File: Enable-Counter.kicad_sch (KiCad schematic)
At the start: 4 parts, among them SW1 SW_Push, U3 SN74LVC112AD, U4 74LVC1G04, U5 74LVC1G04

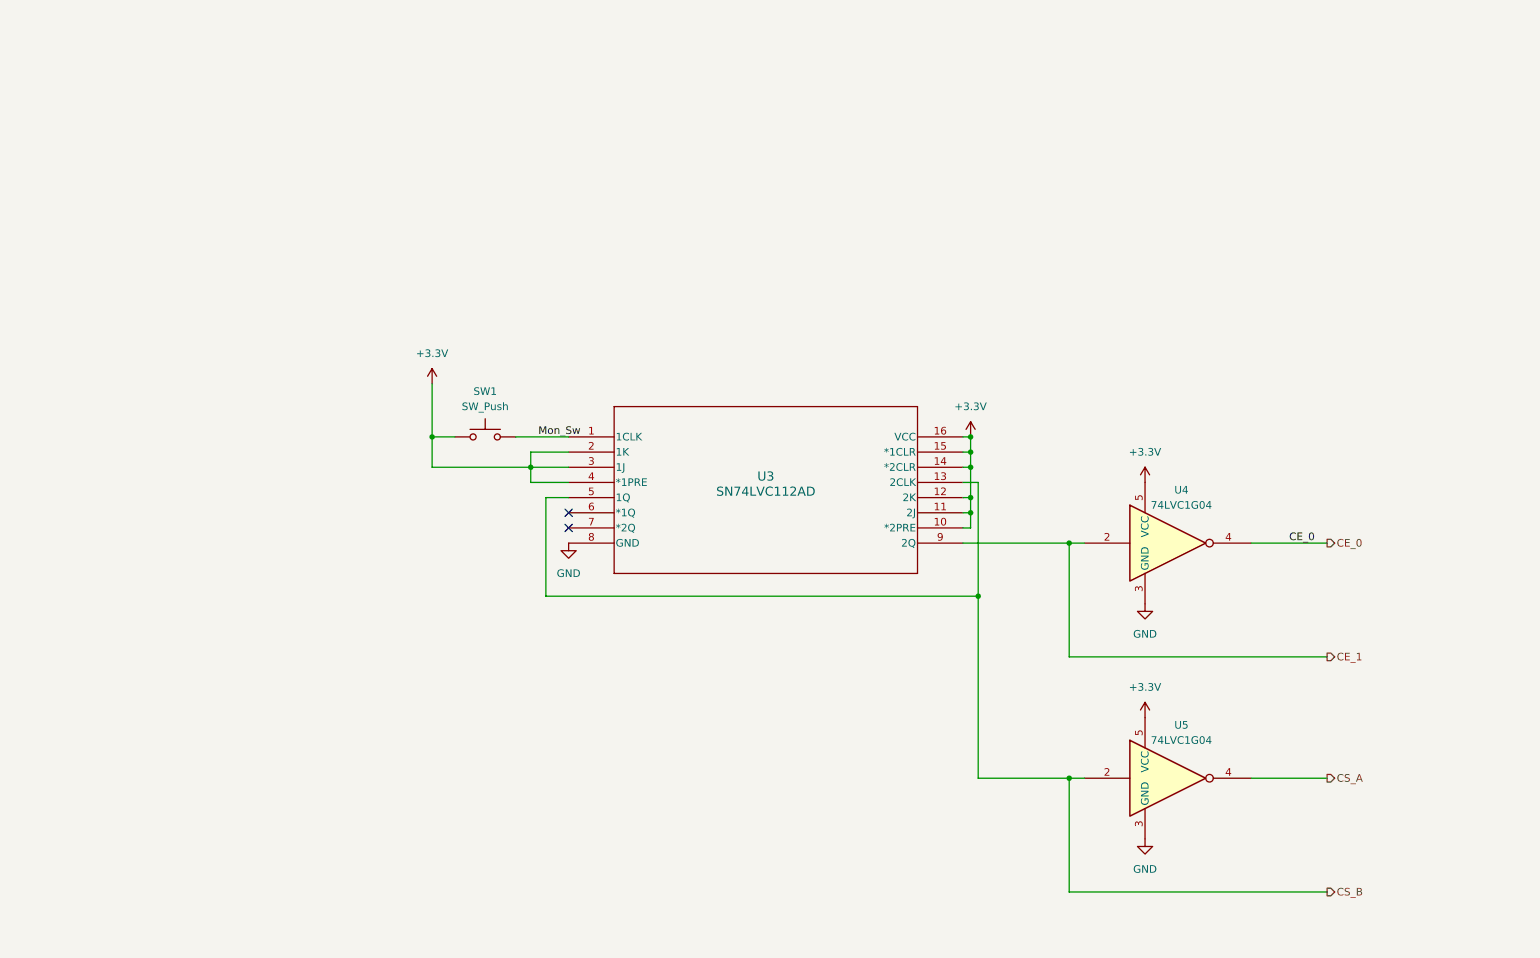
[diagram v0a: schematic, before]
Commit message: Switch debounce, input mDP to switch ICs
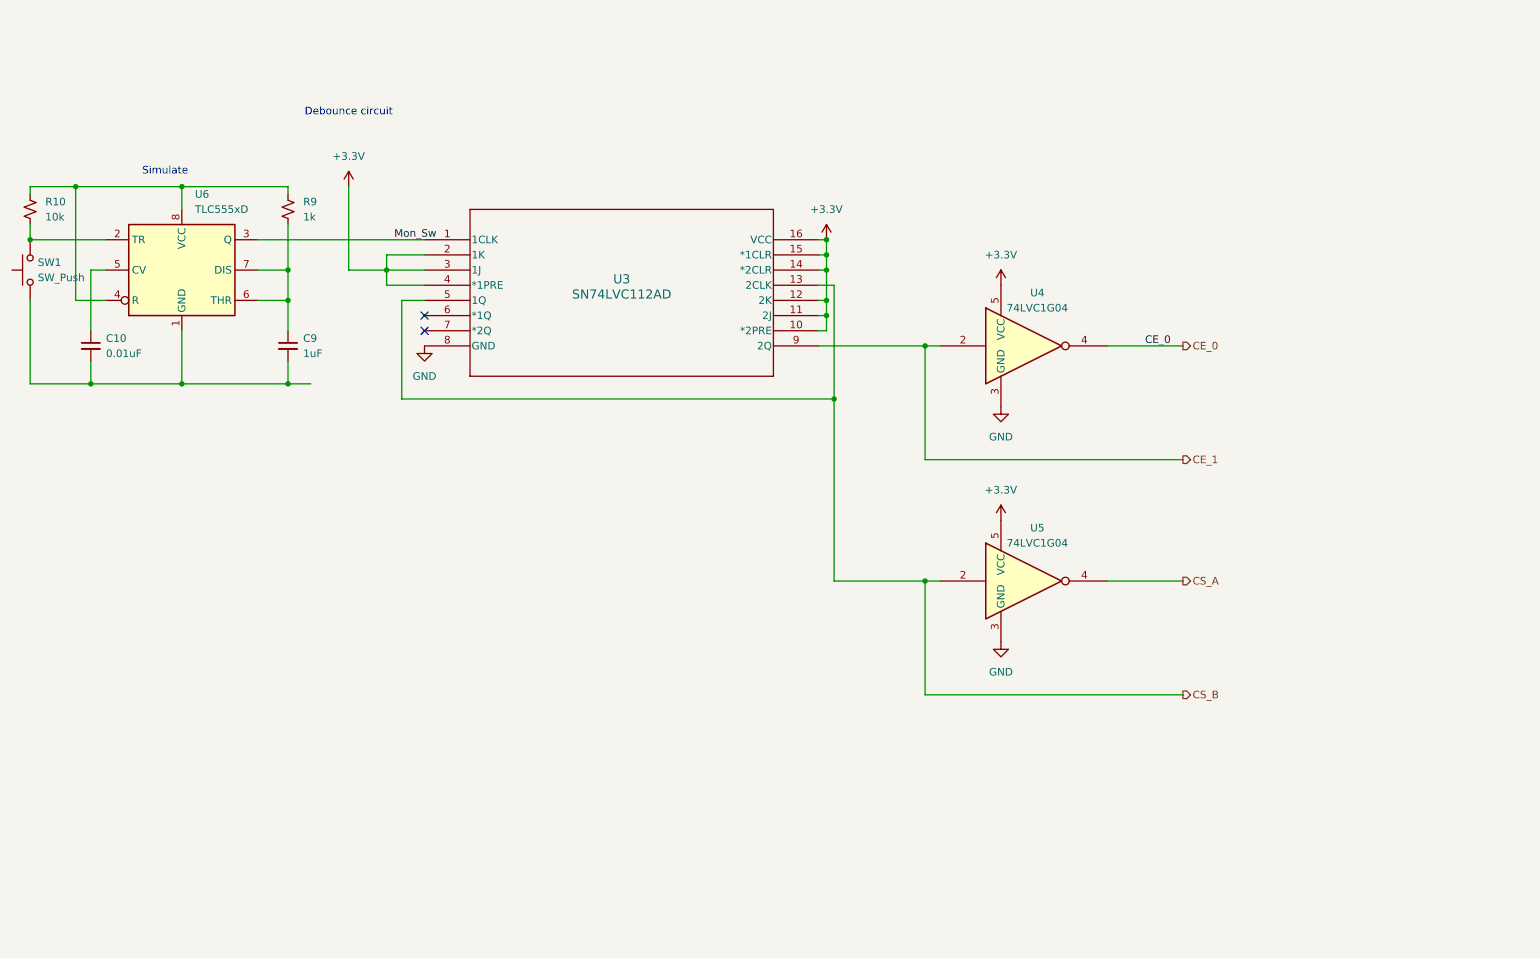
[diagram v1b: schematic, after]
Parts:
- added C10: 0.01uF, symbol Device:C_Small
- added C9: 1uF, symbol Device:C_Small
- added R10: 10k, symbol Device:R_Small_US
- added R9: 1k, symbol Device:R_Small_US
- added U6: TLC555xD, Package_SO:SOIC-8_3.9x4.9mm_P1.27mm, symbol Timer:TLC555xD
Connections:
- net +3.3V: no longer SW1.1
- net Mon_Sw: now also U6.3 (Q); no longer SW1.2
- new net: C10.2, C9.2, SW1.1, U6.1 (GND)
- new net: R10.2, SW1.2, U6.2 (TR)
- new net: C9.1, R9.2, U6.6 (THR), U6.7 (DIS)
- new net: R10.1, R9.1, U6.4 (R), U6.8 (VCC)
- new net: C10.1, U6.5 (CV)
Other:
- note added: "Debounce circuit"
- note added: "Simulate"
- moved on the sheet: U3, U4, U5

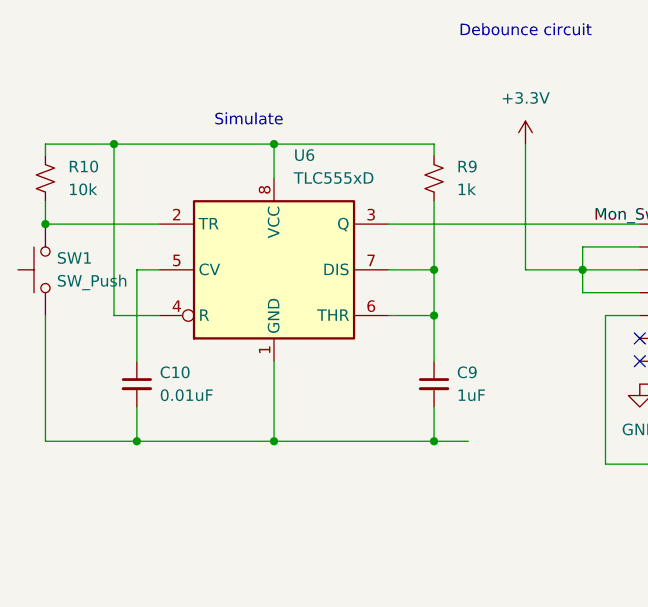
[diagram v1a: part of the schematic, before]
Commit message: Fix debounce circuit
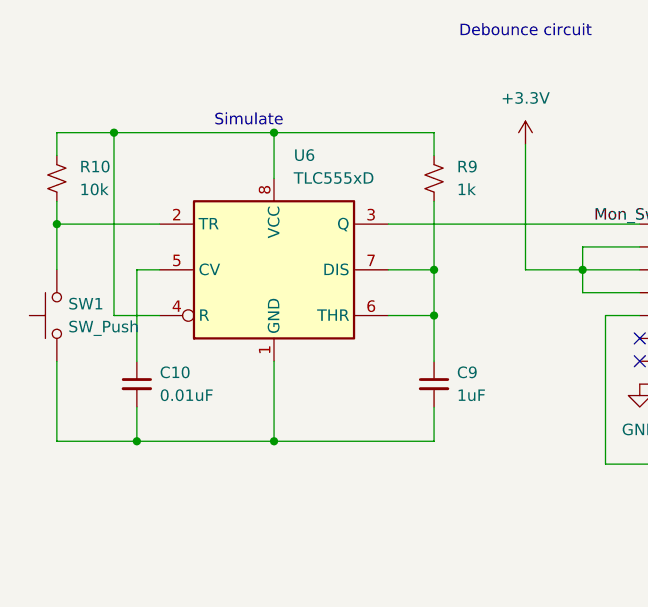
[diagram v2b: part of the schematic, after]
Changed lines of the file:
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@@
 	(paper "USLetter")
+	(junction
+		(at 41.91 41.91)
+		(diameter 0)
+		(color 0 0 0 0)
+	)
 	(junction
 		(at 149.86 57.15)
@@
 	)
 	(junction
+		(at 24.13 41.91)
+		(diameter 0)
+		(color 0 0 0 0)
+	)
+	(junction
 		(at 59.69 57.15)
 		(diameter 0)
@@
 	)
 	(junction
+		(at 17.78 52.07)
+		(diameter 0)
+		(color 0 0 0 0)
+	)
+	(junction
 		(at 151.13 78.74)
 		(diameter 0)
@@
 	)
 	(junction
-		(at 59.69 76.2)
-		(diameter 0)
-		(color 0 0 0 0)
-	)
-	(junction
-		(at 16.51 52.07)
-		(diameter 0)
-		(color 0 0 0 0)
-	)
-	(junction
 		(at 26.67 76.2)
 		(diameter 0)
@@
 		(color 0 0 0 0)
 	)
-	(junction
-		(at 24.13 43.18)
-		(diameter 0)
-		(color 0 0 0 0)
-	)
-	(junction
-		(at 41.91 43.18)
-		(diameter 0)
-		(color 0 0 0 0)
-	)
 	(no_connect
 		(at 82.55 67.31)
@@
 	(wire
 		(pts
+			(xy 17.78 67.31) (xy 17.78 76.2)
+		)
+		(stroke
+			(width 0)
+			(type default)
+		)
+	)
+	(wire
+		(pts
 			(xy 76.2 59.69) (xy 82.55 59.69)
 		)
@@
 	(wire
 		(pts
-			(xy 41.91 43.18) (xy 59.69 43.18)
+			(xy 41.91 41.91) (xy 59.69 41.91)
 		)
 		(stroke
@@
 	(wire
 		(pts
+			(xy 17.78 52.07) (xy 17.78 57.15)
+		)
+		(stroke
+			(width 0)
+			(type default)
+		)
+	)
+	(wire
+		(pts
+			(xy 17.78 41.91) (xy 17.78 44.45)
+		)
+		(stroke
+			(width 0)
+			(type default)
+		)
+	)
+	(wire
+		(pts
+			(xy 17.78 49.53) (xy 17.78 52.07)
+		)
+		(stroke
+			(width 0)
+			(type default)
+		)
+	)
+	(wire
+		(pts
 			(xy 69.85 43.18) (xy 69.85 57.15)
 		)
@@
 	(wire
 		(pts
-			(xy 16.51 49.53) (xy 16.51 52.07)
-		)
-		(stroke
-			(width 0)
-			(type default)
-		)
-	)
-	(wire
-		(pts
 			(xy 76.2 54.61) (xy 76.2 57.15)
 		)
@@
 	(wire
 		(pts
+			(xy 17.78 76.2) (xy 26.67 76.2)
+		)
+		(stroke
+			(width 0)
+			(type default)
+		)
+	)
+	(wire
+		(pts
 			(xy 166.37 69.85) (xy 166.37 88.9)
 		)
@@
 	(wire
 		(pts
-			(xy 24.13 43.18) (xy 41.91 43.18)
-		)
-		(stroke
-			(width 0)
-			(type default)
-		)
-	)
-	(wire
-		(pts
-			(xy 16.51 76.2) (xy 26.67 76.2)
+			(xy 24.13 41.91) (xy 41.91 41.91)
 		)
 		(stroke
@@
 	(wire
 		(pts
-			(xy 16.51 52.07) (xy 29.21 52.07)
-		)
-		(stroke
-			(width 0)
-			(type default)
-		)
-	)
-	(wire
-		(pts
-			(xy 59.69 76.2) (xy 63.5 76.2)
+			(xy 17.78 52.07) (xy 29.21 52.07)
 		)
 		(stroke
@@
 	(wire
 		(pts
+			(xy 17.78 41.91) (xy 24.13 41.91)
+		)
+		(stroke
+			(width 0)
+			(type default)
+		)
+	)
+	(wire
+		(pts
 			(xy 29.21 62.23) (xy 24.13 62.23)
 		)
@@
 	(wire
 		(pts
-			(xy 16.51 44.45) (xy 16.51 43.18)
-		)
-		(stroke
-			(width 0)
-			(type default)
-		)
-	)
-	(wire
-		(pts
 			(xy 149.86 52.07) (xy 149.86 54.61)
 		)
@@
 	(wire
 		(pts
-			(xy 16.51 62.23) (xy 16.51 76.2)
-		)
-		(stroke
-			(width 0)
-			(type default)
-		)
-	)
-	(wire
-		(pts
-			(xy 41.91 43.18) (xy 41.91 46.99)
+			(xy 41.91 41.91) (xy 41.91 46.99)
 		)
 		(stroke
@@
 	(wire
 		(pts
-			(xy 59.69 43.18) (xy 59.69 44.45)
+			(xy 59.69 41.91) (xy 59.69 44.45)
 		)
 		(stroke
@@
 	(wire
 		(pts
-			(xy 24.13 43.18) (xy 24.13 62.23)
-		)
-		(stroke
-			(width 0)
-			(type default)
-		)
-	)
-	(wire
-		(pts
 			(xy 148.59 59.69) (xy 151.13 59.69)
 		)
@@
 	(wire
 		(pts
-			(xy 16.51 43.18) (xy 24.13 43.18)
-		)
-		(stroke
-			(width 0)
-			(type default)
-		)
-	)
-	(wire
-		(pts
 			(xy 29.21 57.15) (xy 26.67 57.15)
 		)
@@
 		(pts
 			(xy 76.2 57.15) (xy 82.55 57.15)
+		)
+		(stroke
+			(width 0)
+			(type default)
+		)
+	)
+	(wire
+		(pts
+			(xy 24.13 41.91) (xy 24.13 62.23)
 		)
 		(stroke
@@
 	(symbol
 		(lib_id "Switch:SW_Push")
-		(at 16.51 57.15 90)
+		(at 17.78 62.23 90)
 		(unit 1)
 		(exclude_from_sim no)
@@
 		(fields_autoplaced yes)
 		(property "Reference" "SW1"
-			(at 17.78 55.8799 90)
+			(at 19.05 60.9599 90)
 			(effects
 				(font
@@
 		)
 		(property "Value" "SW_Push"
-			(at 17.78 58.4199 90)
+			(at 19.05 63.4999 90)
 			(effects
 				(font
@@
 		)
 		(property "Footprint" ""
-			(at 11.43 57.15 0)
+			(at 12.7 62.23 0)
 			(effects
 				(font
@@
 		)
 		(property "Datasheet" "~"
-			(at 11.43 57.15 0)
+			(at 12.7 62.23 0)
 			(effects
 				(font
@@
 		)
 		(property "Description" "Push button switch, generic, two pins"
-			(at 16.51 57.15 0)
+			(at 17.78 62.23 0)
 			(effects
 				(font
@@
 	)
 	(symbol
+		(lib_id "Device:R_Small_US")
+		(at 17.78 46.99 0)
+		(unit 1)
+		(exclude_from_sim no)
+		(in_bom yes)
+		(on_board yes)
+		(dnp no)
+		(fields_autoplaced yes)
+		(property "Reference" "R10"
+			(at 20.32 45.7199 0)
+			(effects
+				(font
+					(size 1.27 1.27)
+				)
+				(justify left)
+			)
+		)
+		(property "Value" "10k"
+			(at 20.32 48.2599 0)
+			(effects
+				(font
+					(size 1.27 1.27)
+				)
+				(justify left)
+			)
+		)
+		(property "Footprint" ""
+			(at 17.78 46.99 0)
+			(effects
+				(font
+					(size 1.27 1.27)
+				)
+				(hide yes)
+			)
+		)
+		(property "Datasheet" "~"
+			(at 17.78 46.99 0)
+			(effects
+				(font
+					(size 1.27 1.27)
+				)
+				(hide yes)
+			)
+		)
+		(property "Description" "Resistor, small US symbol"
+			(at 17.78 46.99 0)
+			(effects
+				(font
+					(size 1.27 1.27)
+				)
+				(hide yes)
+			)
+		)
+		(pin "2"
+		)
+		(pin "1"
+		)
+		(instances
+			(project "Custom KVM"
+				(path "/0c5b2cf4-6c71-473b-81e1-a704ab2e8eda/a7aaebd5-c008-4775-8536-ee48ae98ac2a"
+					(reference "R10")
+					(unit 1)
+				)
+			)
+		)
+	)
+	(symbol
 		(lib_id "Timer:TLC555xD")
 		(at 41.91 57.15 0)
@@
 					(unit 1)
 				)
-			)
-		)
-	)
-	(symbol
-		(lib_id "Device:R_Small_US")
-		(at 16.51 46.99 0)
-		(unit 1)
-		(exclude_from_sim no)
-		(in_bom yes)
-		(on_board yes)
-		(dnp no)
-		(fields_autoplaced yes)
-		(property "Reference" "R10"
-			(at 19.05 45.7199 0)
-			(effects
-				(font
-					(size 1.27 1.27)
-				)
-				(justify left)
-			)
-		)
-		(property "Value" "10k"
-			(at 19.05 48.2599 0)
-			(effects
-				(font
-					(size 1.27 1.27)
-				)
-				(justify left)
-			)
-		)
-		(property "Footprint" ""
-			(at 16.51 46.99 0)
-			(effects
-				(font
-					(size 1.27 1.27)
-				)
-				(hide yes)
-			)
-		)
-		(property "Datasheet" "~"
-			(at 16.51 46.99 0)
-			(effects
-				(font
-					(size 1.27 1.27)
-				)
-				(hide yes)
-			)
-		)
-		(property "Description" "Resistor, small US symbol"
-			(at 16.51 46.99 0)
-			(effects
-				(font
-					(size 1.27 1.27)
-				)
-				(hide yes)
-			)
-		)
-		(pin "2"
-		)
-		(pin "1"
-		)
-		(instances
-			(project "Custom KVM"
-				(path "/0c5b2cf4-6c71-473b-81e1-a704ab2e8eda/a7aaebd5-c008-4775-8536-ee48ae98ac2a"
-					(reference "R10")
-					(unit 1)
-				)

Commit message: Labels
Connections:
- net GND: now also C10.2, C9.2, SW1.1, U6.1 (GND)
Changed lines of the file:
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@@
+	(wire
+		(pts
+			(xy 41.91 76.2) (xy 41.91 80.01)
+		)
+		(stroke
+			(width 0)
+			(type default)
+		)
+	)
 	(wire
 		(pts
@@
 	(text "Debounce circuit"
 		(exclude_from_sim no)
-		(at 69.85 30.734 0)
+		(at 38.862 37.846 0)
 		(effects
 			(font
@@
 		)
 	)
+	(label "Count_High"
+		(at 153.67 69.85 0)
+		(effects
+			(font
+				(size 1.27 1.27)
+			)
+			(justify left bottom)
+		)
+	)
 	(label "Mon_Sw"
 		(at 77.47 52.07 0)
+		(effects
+			(font
+				(size 1.27 1.27)
+			)
+			(justify left bottom)
+		)
+	)
+	(label "Count_Low"
+		(at 139.7 78.74 0)
 		(effects
 			(font
@@
 		(on_board yes)
 		(dnp no)
-		(fields_autoplaced yes)
 		(property "Reference" "U6"
-			(at 44.1041 44.45 0)
+			(at 40.386 57.15 0)
 			(effects
 				(font
@@
 					(unit 1)
 				)
+			)
+		)
+	)
+	(symbol
+		(lib_name "GND_1")
+		(lib_id "power:GND")
+		(at 41.91 80.01 0)
+		(unit 1)
+		(exclude_from_sim no)
+		(in_bom yes)
+		(on_board yes)
+		(dnp no)
+		(fields_autoplaced yes)
+		(property "Reference" "#PWR17"
+			(at 41.91 86.36 0)
+			(effects
+				(font
+					(size 1.27 1.27)
+				)
+				(hide yes)
+			)
+		)
+		(property "Value" "GND"
+			(at 41.91 85.09 0)
+			(effects
+				(font
+					(size 1.27 1.27)
+				)
+			)
+		)
+		(property "Footprint" ""
+			(at 41.91 80.01 0)
+			(effects
+				(font
+					(size 1.27 1.27)
+				)
+				(hide yes)
+			)
+		)
+		(property "Datasheet" ""
+			(at 41.91 80.01 0)
+			(effects
+				(font
+					(size 1.27 1.27)
+				)
+				(hide yes)
+			)
+		)
+		(property "Description" "Power symbol creates a global label with name \"GND\" , ground"
+			(at 41.91 80.01 0)
+			(effects
+				(font
+					(size 1.27 1.27)
+				)
+				(hide yes)
+			)
+		)
+		(pin "1"
+		)
+		(instances
+			(project "Custom KVM"
+				(path "/0c5b2cf4-6c71-473b-81e1-a704ab2e8eda/a7aaebd5-c008-4775-8536-ee48ae98ac2a"
+					(reference "#PWR17")
+					(unit 1)
+				)
